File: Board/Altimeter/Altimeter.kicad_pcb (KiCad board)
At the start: 2 copper layers, 40 x 40 mm, 53 parts, among them J1 PWRIN, J2 STLink, J3 Micro_SD_Card_Det_Hirose_DM3AT, J4 GNSS, J5 RS485, J6 ReleaseSys, SW1 SW_RESET, U1 STM32L431RBTx, U2 LPS22HB_Module, U3 ST1480AxDR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

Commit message: almost complete (size:50x30) task: silk and via
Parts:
- removed the REF** at (167.2, 62.8)
- removed the REF** at (167.2, 97.2)
- removed the REF** at (132.8, 97.2)
- added REF**: MountingHole_3.2mm_M3, Mounting_Holes:MountingHole_3.2mm_M3, F.Cu at (172.3, 72.8)
- added REF**: MountingHole_3.2mm_M3, Mounting_Holes:MountingHole_3.2mm_M3, F.Cu at (172.2, 97.2)
- added REF**: MountingHole_3.2mm_M3, Mounting_Holes:MountingHole_3.2mm_M3, F.Cu at (127.8, 97.2)
- R14, R15: moved to B.Cu
- R2, R3, R4, R5: moved to F.Cu
- moved D5 20.2 mm to (148.7, 89.0), turned to 180 degrees
- moved R4 18.9 mm to (148.5, 90.5), turned to 180 degrees
- moved J4 18.7 mm to (138.1, 71.6)
- moved R5 17.5 mm to (151.5, 89.0), turned to 180 degrees
- moved D3 17.2 mm to (148.7, 91.9), turned to 180 degrees
- moved D4 16.1 mm to (151.3, 90.5), turned to 180 degrees
- moved R2 16.1 mm to (148.5, 93.4), turned to 180 degrees
- moved R3 14.4 mm to (151.5, 91.9), turned to 180 degrees
- moved R15 13.8 mm to (150.0, 77.0), turned to 90 degrees
- moved R14 13.8 mm to (147.5, 77.0), turned to 90 degrees
- moved D2 13.3 mm to (151.3, 93.4), turned to 180 degrees
- moved J6 11.6 mm to (161.9, 71.6)
- moved REF** 11.2 mm to (127.8, 72.8)
- moved U2 10.3 mm to (150.0, 78.0)
- moved U3 9.56 mm to (147.8, 97.0)
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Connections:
- D2 pad 1: Net-(D2-Pad1) -> GND
- D2 pad 2: /LED_R -> Net-(D2-Pad2)
- D4 pad 1: Net-(D4-Pad1) -> GND
- D4 pad 2: /LED_G -> Net-(D4-Pad2)
- J2 pad 2: /SWDIO -> /RESET
- J2 pad 3: /SWCLK -> /SWDIO
- J2 pad 4: /RESET -> /SWCLK
- J6 pad 3: (no net) -> /TRIGGER
- J6 pad 4: (no net) -> /BUZZER
- J6 pad 5: (no net) -> /FLIGHTPIN
- R2 pad 1: GND -> Net-(D2-Pad2)
- R2 pad 2: Net-(D2-Pad1) -> /LED_R
- R4 pad 1: GND -> Net-(D4-Pad2)
- R4 pad 2: Net-(D4-Pad1) -> /LED_G
- U1 pad 23: /RS485_EN -> (no net)
- U1 pad 24: /RS485_TX -> (no net)
- U1 pad 25: /RS485_RX -> (no net)
- U1 pad 28: (no net) -> /RS485_EN
- U1 pad 29: (no net) -> /RS485_TX
- U1 pad 30: (no net) -> /RS485_RX
- U1 pad 42: (no net) -> /FLIGHTPIN
- U1 pad 43: (no net) -> /BUZZER
- U1 pad 44: (no net) -> /TRIGGER
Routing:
- net +3V3: track 101.7 -> 150.2 mm, vias 8 -> 9
- net /FLIGHTPIN: track 0.00 -> 32.1 mm
- net /BUZZER: track 0.00 -> 30.7 mm
- net /TRIGGER: track 0.00 -> 29.4 mm
- net /I2C1_SCL: track 0.00 -> 23.1 mm, vias 0 -> 1
- net /I2C1_SDA: track 0.00 -> 21.3 mm, vias 0 -> 1
- net /LED_B: track 22.1 -> 3.80 mm
- net /GNSS_1PPS: track 28.4 -> 11.1 mm
- net /SD_CMD: track 12.4 -> 29.1 mm, vias 1 -> 2
- net /GNSS_TX: track 26.9 -> 10.5 mm
- net /LED_G: track 20.5 -> 4.17 mm
- net /GNSS_RX: track 25.6 -> 9.84 mm
- net Net-(J3-Pad5): track 5.18 -> 19.8 mm, vias 0 -> 2
- net /LED_Y: track 19.0 -> 5.38 mm
- net /LED_R: track 17.5 -> 5.97 mm
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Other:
- board size 40 x 40 mm -> 50 x 30 mm

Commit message: minor update and bug fix
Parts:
- added C16: 0.1u, Capacitors_SMD:C_0603, B.Cu at (167.8, 90.2)
- added C17: 0.47u, Capacitors_SMD:C_0805, B.Cu at (167.3, 87.0)
- added D6: RSX101VA, Diodes_SMD:D_TUMD2, B.Cu at (167.8, 97.2)
- added D7: RSX101VA, Diodes_SMD:D_TUMD2, B.Cu at (161.7, 97.2)
- added R16: 10k, Resistors_SMD:R_0603, B.Cu at (161.9, 77.5)
- added R17: 10k, Resistors_SMD:R_0603, B.Cu at (163.9, 77.5)
- added R18: 10k, Resistors_SMD:R_0603, B.Cu at (166.0, 77.5)
- added TP1: MCO, Measurement_Points:Measurement_Point_Round-TH_Small, F.Cu at (154.1, 86.7)
- added VR2: NJM12888, TO_SOT_Packages_SMD:SOT-23-5, B.Cu at (165.4, 89.9)
- R1: moved to B.Cu
- R13: moved to F.Cu
- moved R1 15.4 mm to (172.6, 91.2), turned to 90 degrees
- moved C1 11.8 mm to (155.4, 94.7)
- moved VR1 11.7 mm to (152.9, 94.3)
- moved C2 11.3 mm to (154.9, 91.5)
- moved D1 9.18 mm to (169.6, 93.3), turned to 180 degrees
- moved R13 4.15 mm to (150.8, 97.0), turned to 90 degrees
- moved JP1 1.88 mm to (145.9, 95.7)
- moved U3 1.88 mm to (145.9, 97.0)
- moved C8 0.67 mm to (142.2, 84.0)
- moved C9 0.40 mm to (136.0, 88.2)
- moved C7 0.26 mm to (135.1, 82.8)
- moved C5 0.26 mm to (135.1, 90.7)
- moved C6 0.25 mm to (141.7, 90.7)
- moved C10 0.22 mm to (134.4, 88.5)
- moved C3 0.05 mm to (128.9, 90.6)
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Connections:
- C15 pad 1: +3V3 -> VDD
- J1 pad 1: +6V -> Net-(D6-Pad2)
- J3 pad 4: +3V3 -> VDD
- J5 pad 1: +3V3 -> Net-(D7-Pad2)
- R10 pad 1: +3V3 -> VDD
- R11 pad 1: +3V3 -> VDD
- R7 pad 1: +3V3 -> VDD
- R8 pad 1: +3V3 -> VDD
- R9 pad 1: +3V3 -> VDD
- U1 pad 41: (no net) -> Net-(TP1-Pad1)
- U1 pad 45: /SWDIO -> (no net)
- U1 pad 46: /SWCLK -> /SWDIO
- U1 pad 49: (no net) -> /SWCLK
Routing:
- net +3V3: track 150.2 -> 125.0 mm, vias 9 -> 8
- net +6V: track 8.86 -> 29.3 mm, vias 1 -> 0
- net VDD: track 0.00 -> 19.2 mm, vias 0 -> 1
- net Net-(TP1-Pad1): track 0.00 -> 10.1 mm
- net GND: track 87.0 -> 80.7 mm, vias 111 -> 223
- net /SWCLK: track 21.2 -> 26.8 mm
- net /TRIGGER: track 29.4 -> 34.2 mm
- net /BUZZER: track 30.7 -> 35.5 mm
- net /FLIGHTPIN: track 32.1 -> 36.7 mm
- net Net-(D1-Pad1): track 1.43 -> 3.42 mm, vias 0 -> 1
- net Net-(D7-Pad2): track 0.00 -> 1.86 mm
- net Net-(D6-Pad2): track 0.00 -> 1.86 mm
- net /RS485_RX: track 5.43 -> 3.72 mm
- net /SD_DAT1: track 18.3 -> 17.4 mm
- net /SWDIO: track 24.9 -> 24.1 mm
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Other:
- outline, holes or cut-outs redrawn
- net class Default: via_dia 0.8 -> 0.6; via_drill 0.4 -> 0.3
- rule pad_to_mask_clearance: 0.2 -> 0.16
- rule via_min_size: 0.4 -> 0.5
- board text added: "+3.3V Out"
- board text added: "+6V"
- board text added: "1PPS"
- board text added: "A"
- board text added: "B"
- board text added: "Buzz"
- board text added: "FPin"
- board text added: "GND"
- board text added: "GNSS"
- board text added: "Input 2.7V-6.5V"
- board text added: "PWR"
- board text added: "RS485"
- board text added: "RX"
- board text added: "Release"
- board text added: "Reset"
- board text added: "STLink"
- board text added: "SWD"
- board text added: "TX"
- board text added: "Trig"
- board text added: "UART"
- board text added: "~HalfDuplex"

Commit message: [Altimeter V1.0] add silk of team logo and imprint add gerber files
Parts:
- added G***: LOGO, temp:rask, B.Cu at (146.8, 84.4)
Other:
- board text added: "Baro/GNSS Altimeter"
- board text added: "Baro/GNSS Altimeter V1 @chromium_k 2018.08.10"

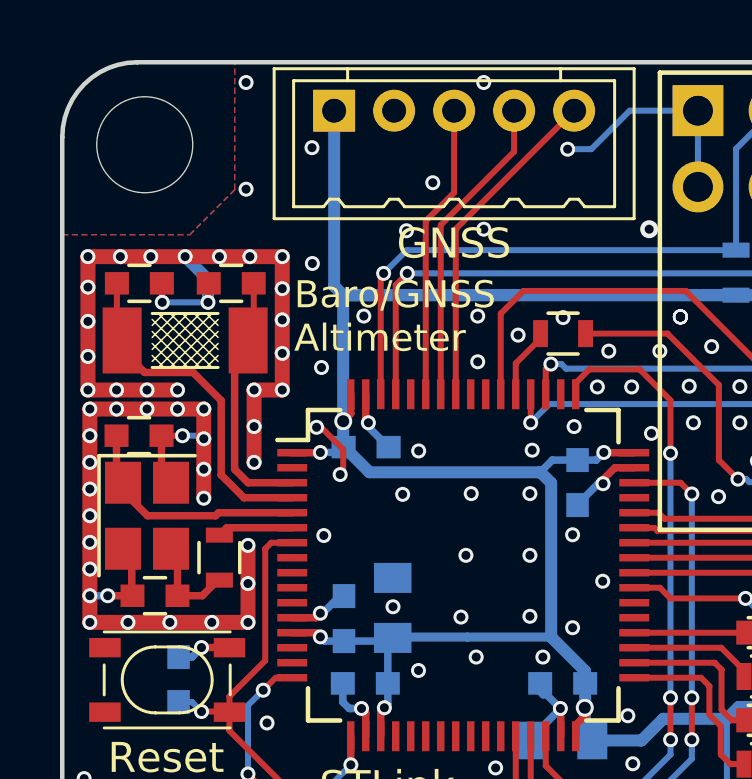
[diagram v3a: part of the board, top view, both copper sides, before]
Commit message: [Altimeter V1.1] invert TX/RX pins of GNSS Connector
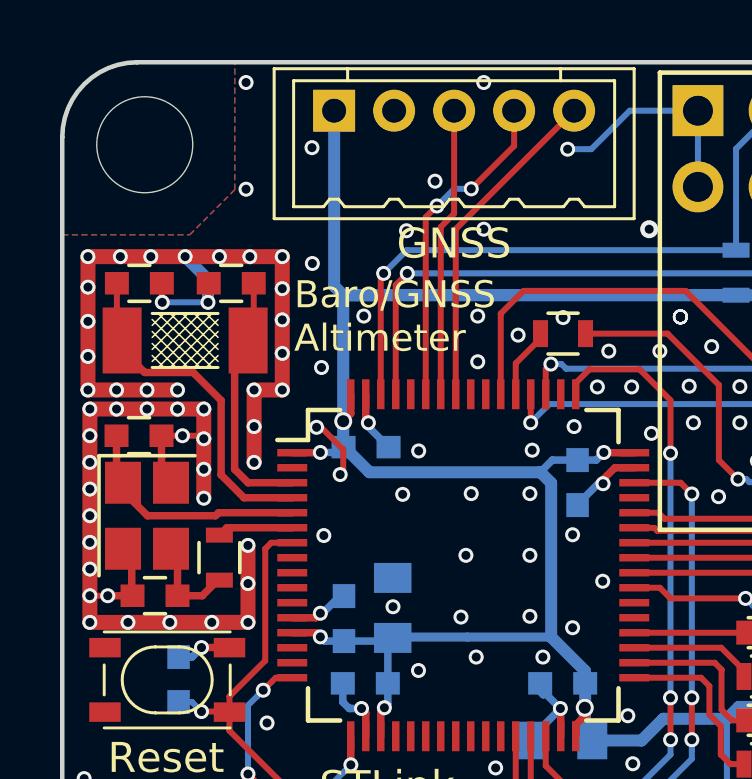
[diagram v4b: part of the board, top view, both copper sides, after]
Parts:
- R14, R15: value 1k -> 10k
- moved G*** 1.18 mm to (148.0, 84.5)
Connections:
- D3 pad 2: /LED_Y -> /LED_G
- D5 pad 2: /LED_B -> /LED_R
- J4 pad 3: /GNSS_RX -> /GNSS_TX
- J4 pad 4: /GNSS_TX -> /GNSS_RX
- R2 pad 2: /LED_R -> /LED_B
- R4 pad 2: /LED_G -> /LED_Y
- U1 pad 33: /LED_R -> /LED_B
- U1 pad 34: /LED_Y -> /LED_G
- U1 pad 35: /LED_G -> /LED_Y
- U1 pad 36: /LED_B -> /LED_R
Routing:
- net /LED_R: track 5.97 -> 3.80 mm
- net /LED_B: track 3.80 -> 5.97 mm
- net /LED_Y: track 5.38 -> 4.17 mm
- net /LED_G: track 4.17 -> 5.38 mm
- net /GNSS_RX: track 9.84 -> 11.0 mm, vias 0 -> 2
- net /GNSS_TX: track 10.5 -> 9.64 mm
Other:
- board text added: "Baro/GNSS Altimeter V1.1 @chromium_k 2018.08.10"
- board text added: "Input 2.9V-6.5V"
- board text removed: "Baro/GNSS Altimeter V1 @chromium_k 2018.08.10"
- board text removed: "Input 2.7V-6.5V"

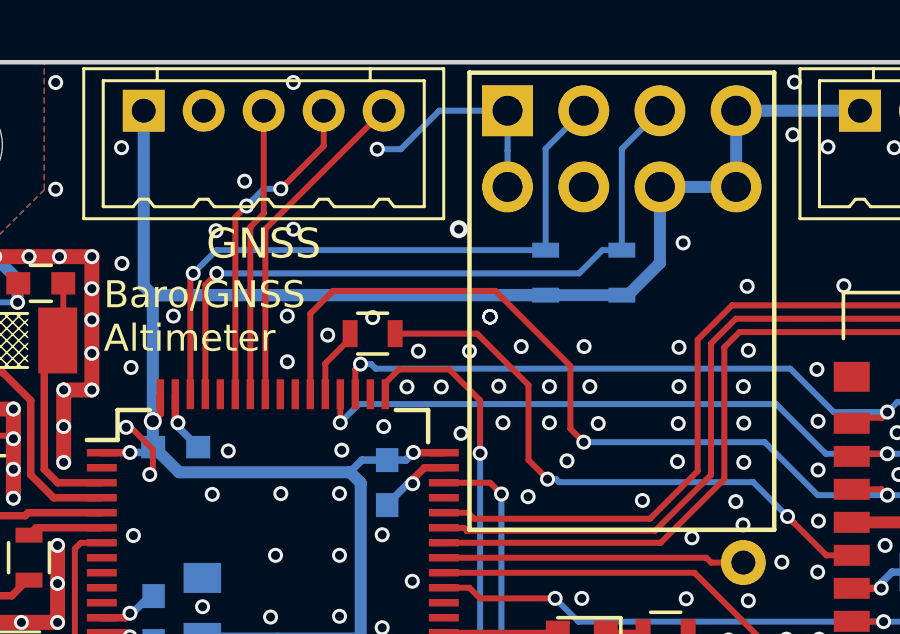
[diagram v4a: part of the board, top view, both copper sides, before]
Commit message: [Altimeter V1.1] connect PH3(BOOT0) to GND add wire between INT_DRDY and MCU
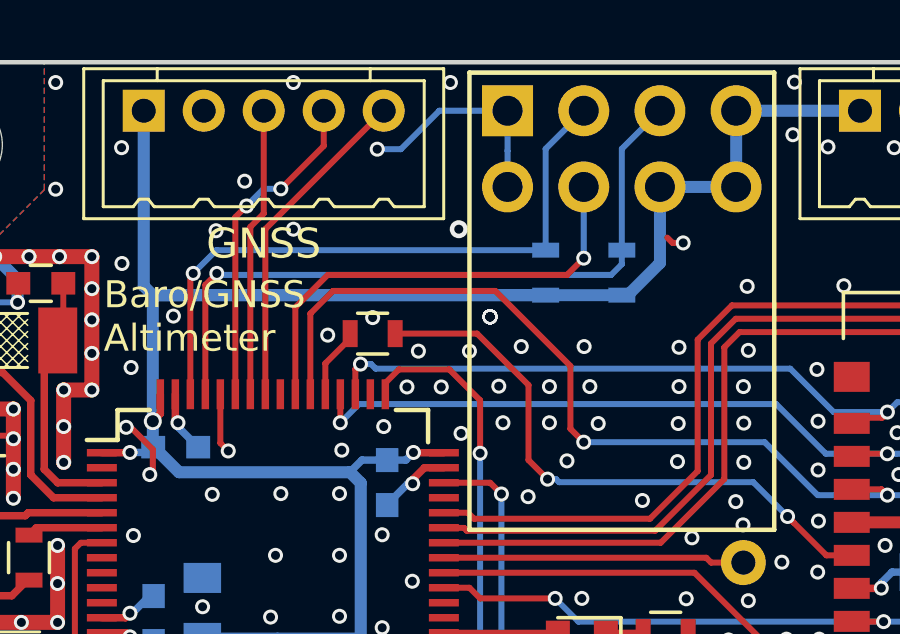
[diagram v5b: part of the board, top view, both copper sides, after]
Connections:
- U1 pad 55: (no net) -> /LPS22HB_INT
- U1 pad 60: (no net) -> GND
- U2 pad 6: (no net) -> /LPS22HB_INT
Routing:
- net /LPS22HB_INT: track 0.00 -> 15.6 mm, vias 0 -> 1
- net GND: track 80.7 -> 83.3 mm, vias 223 -> 222
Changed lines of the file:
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@@
     (thickness 1.6)
     (drawings 60)
-    (tracks 780)
+    (tracks 790)
     (zones 0)
     (modules 63)
-    (nets 47)
+    (nets 48)
   )
   (page A4)
@@
   (net 45 "Net-(D7-Pad2)")
   (net 46 VDD)
+  (net 47 /LPS22HB_INT)
   (net_class Default "これはデフォルトのネット クラスです。"
     (clearance 0.2)
@@
     (add_net /LED_R)
     (add_net /LED_Y)
+    (add_net /LPS22HB_INT)
     (add_net /LSE_IN)
     (add_net /LSE_OUT)
@@
     (pad 7 thru_hole circle (at -1.27 3.81 180) (size 1.7 1.7) (drill 1) (layers *.Cu *.Mask F.SilkS)
       (net 3 +3V3))
-    (pad 6 thru_hole circle (at 1.27 3.81 180) (size 1.7 1.7) (drill 1) (layers *.Cu *.Mask F.SilkS))
+    (pad 6 thru_hole circle (at 1.27 3.81 180) (size 1.7 1.7) (drill 1) (layers *.Cu *.Mask F.SilkS)
+      (net 47 /LPS22HB_INT))
     (pad 5 thru_hole circle (at 3.81 3.81 180) (size 1.7 1.7) (drill 1) (layers *.Cu *.Mask F.SilkS)
       (net 1 GND))
@@
     (pad 61 smd rect (at -2.25 -5.7 90) (size 1 0.25) (layers F.Cu F.Paste F.Mask)
       (net 32 /I2C1_SCL))
-    (pad 60 smd rect (at -1.75 -5.7 90) (size 1 0.25) (layers F.Cu F.Paste F.Mask))
+    (pad 60 smd rect (at -1.75 -5.7 90) (size 1 0.25) (layers F.Cu F.Paste F.Mask)
+      (net 1 GND))
     (pad 59 smd rect (at -1.25 -5.7 90) (size 1 0.25) (layers F.Cu F.Paste F.Mask)
       (net 35 /GNSS_RX))
@@
       (net 37 /GNSS_1PPS))
     (pad 56 smd rect (at 0.25 -5.7 90) (size 1 0.25) (layers F.Cu F.Paste F.Mask))
-    (pad 55 smd rect (at 0.75 -5.7 90) (size 1 0.25) (layers F.Cu F.Paste F.Mask))
+    (pad 55 smd rect (at 0.75 -5.7 90) (size 1 0.25) (layers F.Cu F.Paste F.Mask)
+      (net 47 /LPS22HB_INT))
     (pad 54 smd rect (at 1.25 -5.7 90) (size 1 0.25) (layers F.Cu F.Paste F.Mask)
       (net 25 /SD_CMD))
@@
   (via (at 131.2548 76.4796) (size 0.5) (drill 0.3) (layers F.Cu B.Cu) (net 1))
   (via (at 139.0526 75.5652) (size 0.5) (drill 0.3) (layers F.Cu B.Cu) (net 1))
-  (via (at 138.8494 79.9848) (size 0.5) (drill 0.3) (layers F.Cu B.Cu) (net 1))
   (via (at 141.6942 78.5116) (size 0.5) (drill 0.3) (layers F.Cu B.Cu) (net 1))
   (via (at 140.1956 79.0958) (size 0.5) (drill 0.3) (layers F.Cu B.Cu) (net 1))
@@
   (segment (start 133.477 82.169) (end 133.6294 82.169) (width 0.2) (layer F.Cu) (net 1))
   (segment (start 133.6294 82.169) (end 134.366 82.9056) (width 0.2) (layer F.Cu) (net 1))
-  (via (at 138.8491 78.4606) (size 0.5) (drill 0.3) (layers F.Cu B.Cu) (net 1))
   (via (at 133.6421 80.1751) (size 0.5) (drill 0.3) (layers F.Cu B.Cu) (net 1))
   (via (at 133.3373 76.708) (size 0.5) (drill 0.3) (layers F.Cu B.Cu) (net 1))
@@
   (segment (start 125.921 87.7824) (end 125.9208 87.7826) (width 0.2) (layer F.Cu) (net 1))
   (segment (start 126.5174 87.7824) (end 125.921 87.7824) (width 0.2) (layer F.Cu) (net 1))
+  (segment (start 136.6168 82.6926) (end 136.8806 82.9564) (width 0.2) (layer F.Cu) (net 1))
+  (segment (start 136.6168 81.0666) (end 136.6168 82.6926) (width 0.2) (layer F.Cu) (net 1))
+  (segment (start 151.690847 76.0222) (end 151.513247 75.8446) (width 0.2) (layer F.Cu) (net 1))
+  (segment (start 152.0444 76.0222) (end 151.690847 76.0222) (width 0.2) (layer F.Cu) (net 1))
+  (via (at 144.285 70.675) (size 0.5) (drill 0.3) (layers F.Cu B.Cu) (net 1))
   (segment (start 167.4194 96.1138) (end 167.8308 96.5252) (width 0.5) (layer B.Cu) (net 2))
   (segment (start 161.7348 96.5252) (end 162.1462 96.1138) (width 0.5) (layer B.Cu) (net 2))
@@
   (segment (start 172.593 93.0402) (end 172.6184 93.0402) (width 0.2) (layer F.Cu) (net 9))
   (segment (start 172.6184 93.0402) (end 172.6184 91.9868) (width 0.2) (layer B.Cu) (net 9))
+  (segment (start 147.8644 89.0166) (end 147.8665 89.0145) (width 0.2) (layer F.Cu) (net 10))
+  (segment (start 144.0668 89.0166) (end 147.8644 89.0166) (width 0.2) (layer F.Cu) (net 10))
+  (segment (start 149.4665 91.9355) (end 150.7105 91.9355) (width 0.2) (layer F.Cu) (net 11))
+  (segment (start 147.726 90.275) (end 147.726 90.475) (width 0.2) (layer F.Cu) (net 12))
+  (segment (start 146.9676 89.5166) (end 147.726 90.275) (width 0.2) (layer F.Cu) (net 12))
+  (segment (start 144.0668 89.5166) (end 146.9676 89.5166) (width 0.2) (layer F.Cu) (net 12))
+  (segment (start 147.333 91.9355) (end 147.8665 91.9355) (width 0.2) (layer F.Cu) (net 13))
+  (segment (start 146.9774 91.5799) (end 147.333 91.9355) (width 0.2) (layer F.Cu) (net 13))
+  (segment (start 146.9774 90.2464) (end 146.9774 91.5799) (width 0.2) (layer F.Cu) (net 13))
+  (segment (start 144.0668 90.0166) (end 146.7476 90.0166) (width 0.2) (layer F.Cu) (net 13))
+  (segment (start 146.7476 90.0166) (end 146.9774 90.2464) (width 0.2) (layer F.Cu) (net 13))
   (segment (start 147.2695 93.396) (end 147.726 93.396) (width 0.2) (layer F.Cu) (net 14))
   (segment (start 146.2951 90.5166) (end 146.571 90.7925) (width 0.2) (layer F.Cu) (net 14))
@@
   (segment (start 146.571 91.745) (end 146.952 92.126) (width 0.2) (layer F.Cu) (net 14))
   (segment (start 146.952 93.0785) (end 147.2695 93.396) (width 0.2) (layer F.Cu) (net 14))
-  (segment (start 149.4665 91.9355) (end 150.7105 91.9355) (width 0.2) (layer F.Cu) (net 11))
-  (segment (start 147.333 91.9355) (end 147.8665 91.9355) (width 0.2) (layer F.Cu) (net 13))
-  (segment (start 146.9774 91.5799) (end 147.333 91.9355) (width 0.2) (layer F.Cu) (net 13))
-  (segment (start 146.9774 90.2464) (end 146.9774 91.5799) (width 0.2) (layer F.Cu) (net 13))
-  (segment (start 144.0668 90.0166) (end 146.7476 90.0166) (width 0.2) (layer F.Cu) (net 13))
-  (segment (start 146.7476 90.0166) (end 146.9774 90.2464) (width 0.2) (layer F.Cu) (net 13))
-  (segment (start 147.726 90.275) (end 147.726 90.475) (width 0.2) (layer F.Cu) (net 12))
-  (segment (start 146.9676 89.5166) (end 147.726 90.275) (width 0.2) (layer F.Cu) (net 12))
-  (segment (start 144.0668 89.5166) (end 146.9676 89.5166) (width 0.2) (layer F.Cu) (net 12))
-  (segment (start 147.8644 89.0166) (end 147.8665 89.0145) (width 0.2) (layer F.Cu) (net 10))
-  (segment (start 144.0668 89.0166) (end 147.8644 89.0166) (width 0.2) (layer F.Cu) (net 10))
   (segment (start 149.4665 89.0145) (end 150.7105 89.0145) (width 0.2) (layer F.Cu) (net 15))
   (via (at 145.986496 84.3915) (size 0.5) (drill 0.3) (layers F.Cu B.Cu) (net 16))
@@
   (segment (start 147.46 76.263) (end 147.46 72.8855) (width 0.2) (layer B.Cu) (net 31))
   (via (at 136.4996 77.0382) (size 0.5) (drill 0.3) (layers F.Cu B.Cu) (net 32))
-  (segment (start 150 76.263) (end 149.35 76.263) (width 0.2) (layer B.Cu) (net 32))
-  (segment (start 149.35 76.263) (end 148.5748 77.0382) (width 0.2) (layer B.Cu) (net 32))
   (segment (start 136.1168 81.0666) (end 136.1168 77.421) (width 0.2) (layer F.Cu) (net 32))
   (segment (start 136.4996 77.0382) (end 136.1168 77.421) (width 0.2) (layer F.Cu) (net 32))
-  (segment (start 136.4996 77.0382) (end 148.5748 77.0382) (width 0.2) (layer B.Cu) (net 32))
   (segment (start 150 72.8855) (end 151.27 71.6155) (width 0.2) (layer B.Cu) (net 32))
   (segment (start 150 76.263) (end 150 72.8855) (width 0.2) (layer B.Cu) (net 32))
+  (segment (start 136.5506 77.0892) (end 136.4996 77.0382) (width 0.2) (layer B.Cu) (net 32))
+  (segment (start 149.6444 77.0892) (end 136.5506 77.0892) (width 0.2) (layer B.Cu) (net 32))
+  (segment (start 150 76.263) (end 150 76.7336) (width 0.2) (layer B.Cu) (net 32))
+  (segment (start 150 76.7336) (end 149.6444 77.0892) (width 0.2) (layer B.Cu) (net 32))
   (segment (start 140.6168 92.4666) (end 140.6168 95.1889) (width 0.2) (layer F.Cu) (net 33))
   (segment (start 141.6939 97.8407) (end 142.7102 98.857) (width 0.2) (layer F.Cu) (net 33))
@@
   (segment (start 166.2844 86.995) (end 166.2971 87.0077) (width 0.5) (layer B.Cu) (net 46))
   (segment (start 161.7566 86.995) (end 166.2844 86.995) (width 0.5) (layer B.Cu) (net 46))
+  (via (at 148.73 76.5304) (size 0.5) (drill 0.3) (layers F.Cu B.Cu) (net 47))
+  (segment (start 139.1168 78.168) (end 139.1168 81.0666) (width 0.2) (layer F.Cu) (net 47))
+  (segment (start 140.1956 77.0892) (end 139.1168 78.168) (width 0.2) (layer F.Cu) (net 47))
+  (segment (start 148.73 76.5304) (end 148.1712 77.0892) (width 0.2) (layer F.Cu) (net 47))
+  (segment (start 148.1712 77.0892) (end 140.1956 77.0892) (width 0.2) (layer F.Cu) (net 47))
+  (segment (start 148.73 76.5304) (end 148.73 74.1555) (width 0.2) (layer B.Cu) (net 47))
   (zone (net 1) (net_name GND) (layer B.Cu) (hatch edge 0.508)
     (connect_pads (clearance 0.254))
@@
       )
     )
+  )
+  (zone (net 0) (net_name "") (layer F.Cu) (hatch edge 0.508)
+    (connect_pads (clearance 0.254))
+    (min_thickness 0.254)
+    (keepout (tracks allowed) (vias allowed) (copperpour not_allowed))
+    (fill (arc_segments 16) (thermal_gap 0.508) (thermal_bridge_width 0.508))
+    (polygon
+      (pts
+        (xy 138.3414 76.7336) (xy 140.2718 76.7336) (xy 139.5098 78.4354) (xy 138.3414 78.4354)
+      )
+    )
